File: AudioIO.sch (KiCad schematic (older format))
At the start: 39 parts, among them U4 TL074

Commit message: Chanced regulators and oscillator work.
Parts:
- C32: renamed from C17; footprint Capacitor_SMD:C_0603_1608Metric -> Capacitor_SMD:C_0402_1005Metric
- C33: renamed from C18; footprint Capacitor_SMD:C_0603_1608Metric -> Capacitor_SMD:C_0402_1005Metric
- C34: renamed from C19; footprint Capacitor_SMD:C_0603_1608Metric -> Capacitor_SMD:C_0402_1005Metric
- C35: renamed from C20; footprint Capacitor_SMD:C_0603_1608Metric -> Capacitor_SMD:C_0402_1005Metric
- renumbered C15 to C30, C16 to C31, C21 to C36, C22 to C37, C23 to C38, C24 to C39, C25 to C40, C26 to C41, C27 to C42, C28 to C43, R7 to R10, R8 to R11, R9 to R12, R10 to R13, R11 to R14, R12 to R15, R13 to R16, R14 to R17, R15 to R18, R16 to R19, R17 to R20, R18 to R21, R19 to R22, R20 to R23, R21 to R24, R22 to R25, R3 to R6, R4 to R7, R5 to R8, R6 to R9, U4 to U5

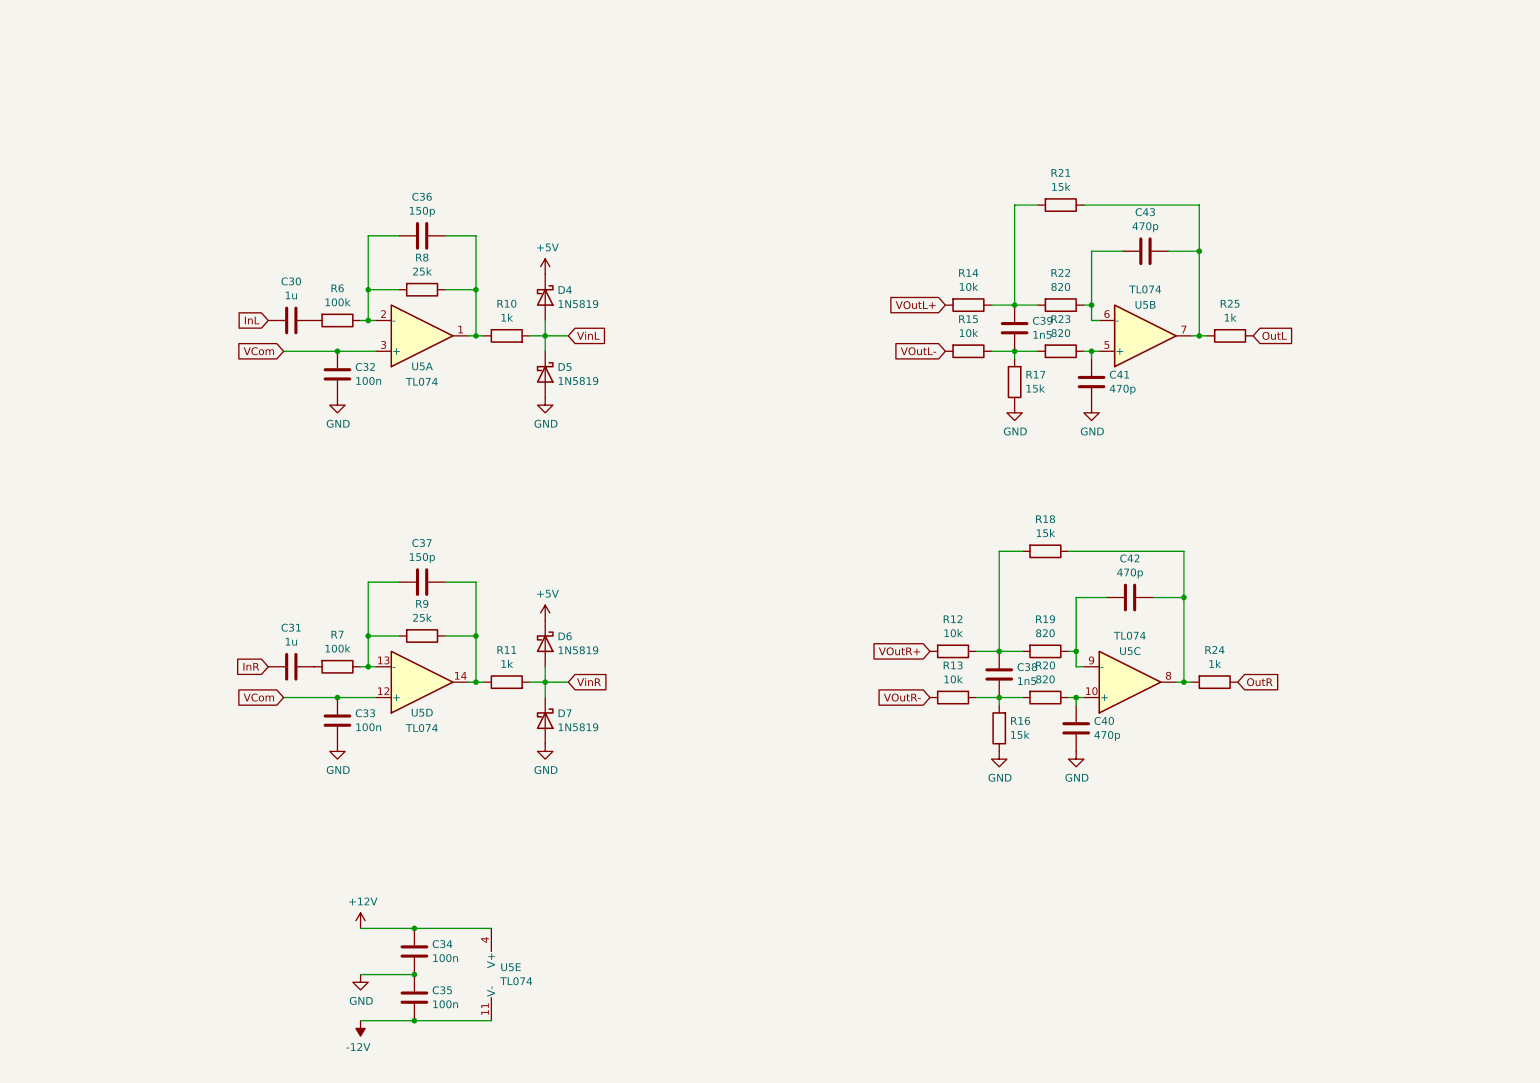
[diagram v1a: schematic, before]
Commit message: Added UI components.
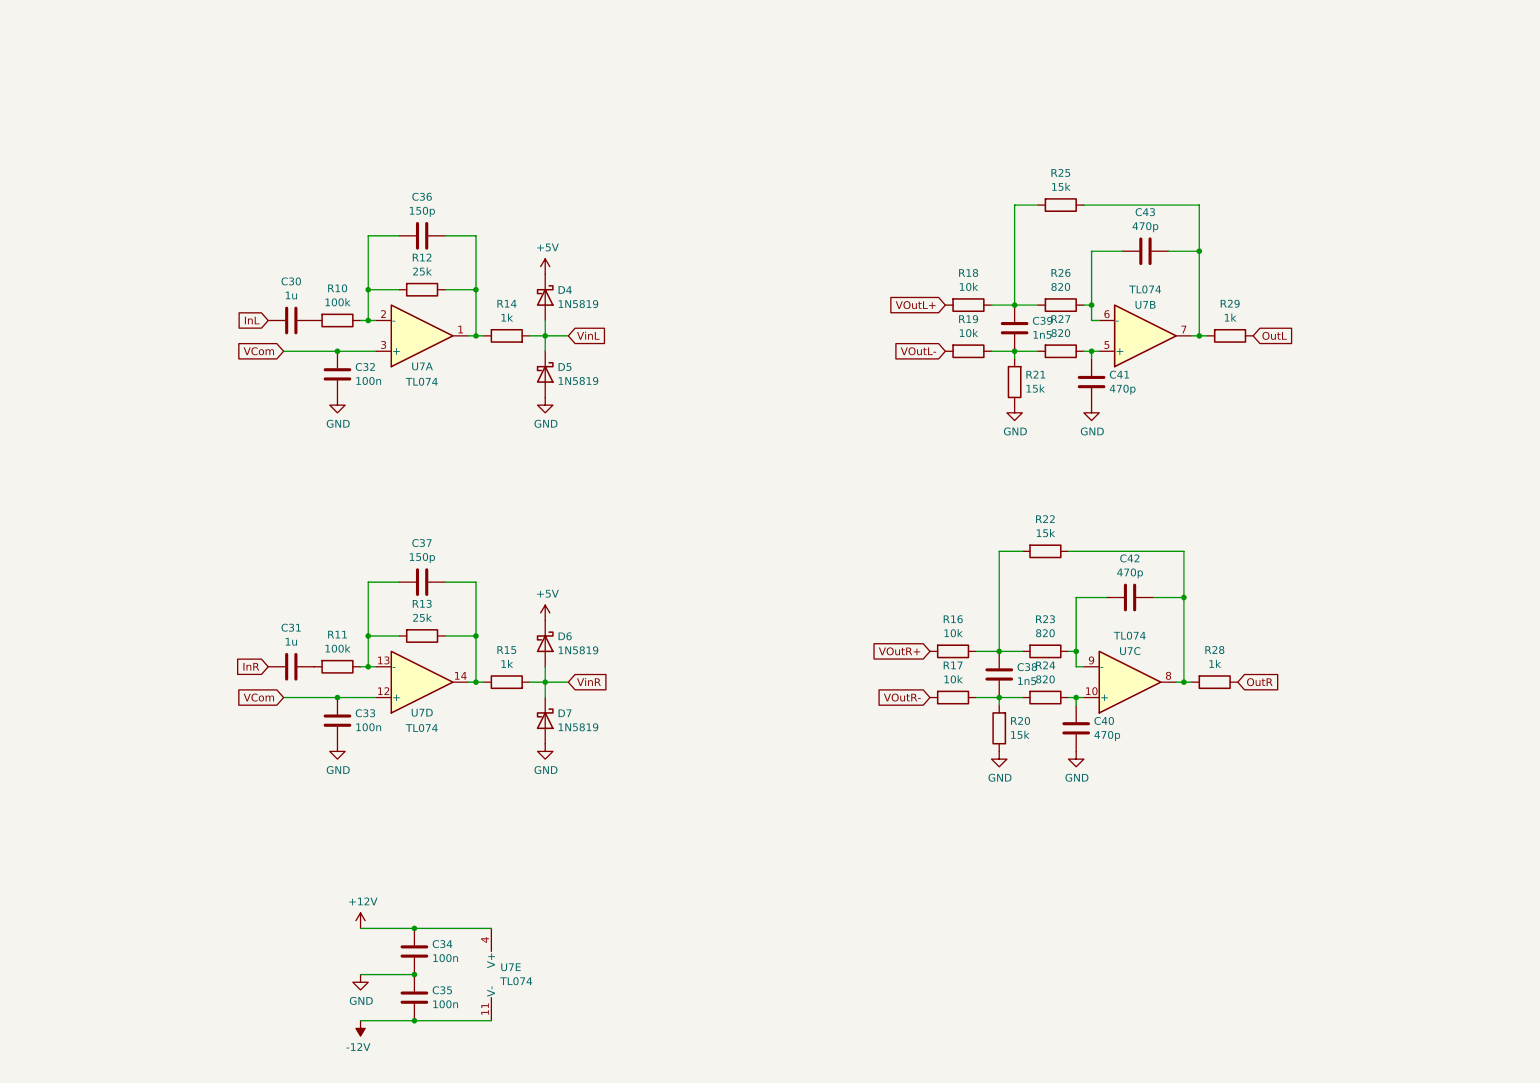
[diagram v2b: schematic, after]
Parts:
- renumbered R6 to R10, R7 to R11, R8 to R12, R9 to R13, R10 to R14, R11 to R15, R12 to R16, R13 to R17, R14 to R18, R15 to R19, R16 to R20, R17 to R21, R18 to R22, R19 to R23, R20 to R24, R21 to R25, R22 to R26, R23 to R27, R24 to R28, R25 to R29, U5 to U7

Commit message: Moved codec to audio module.
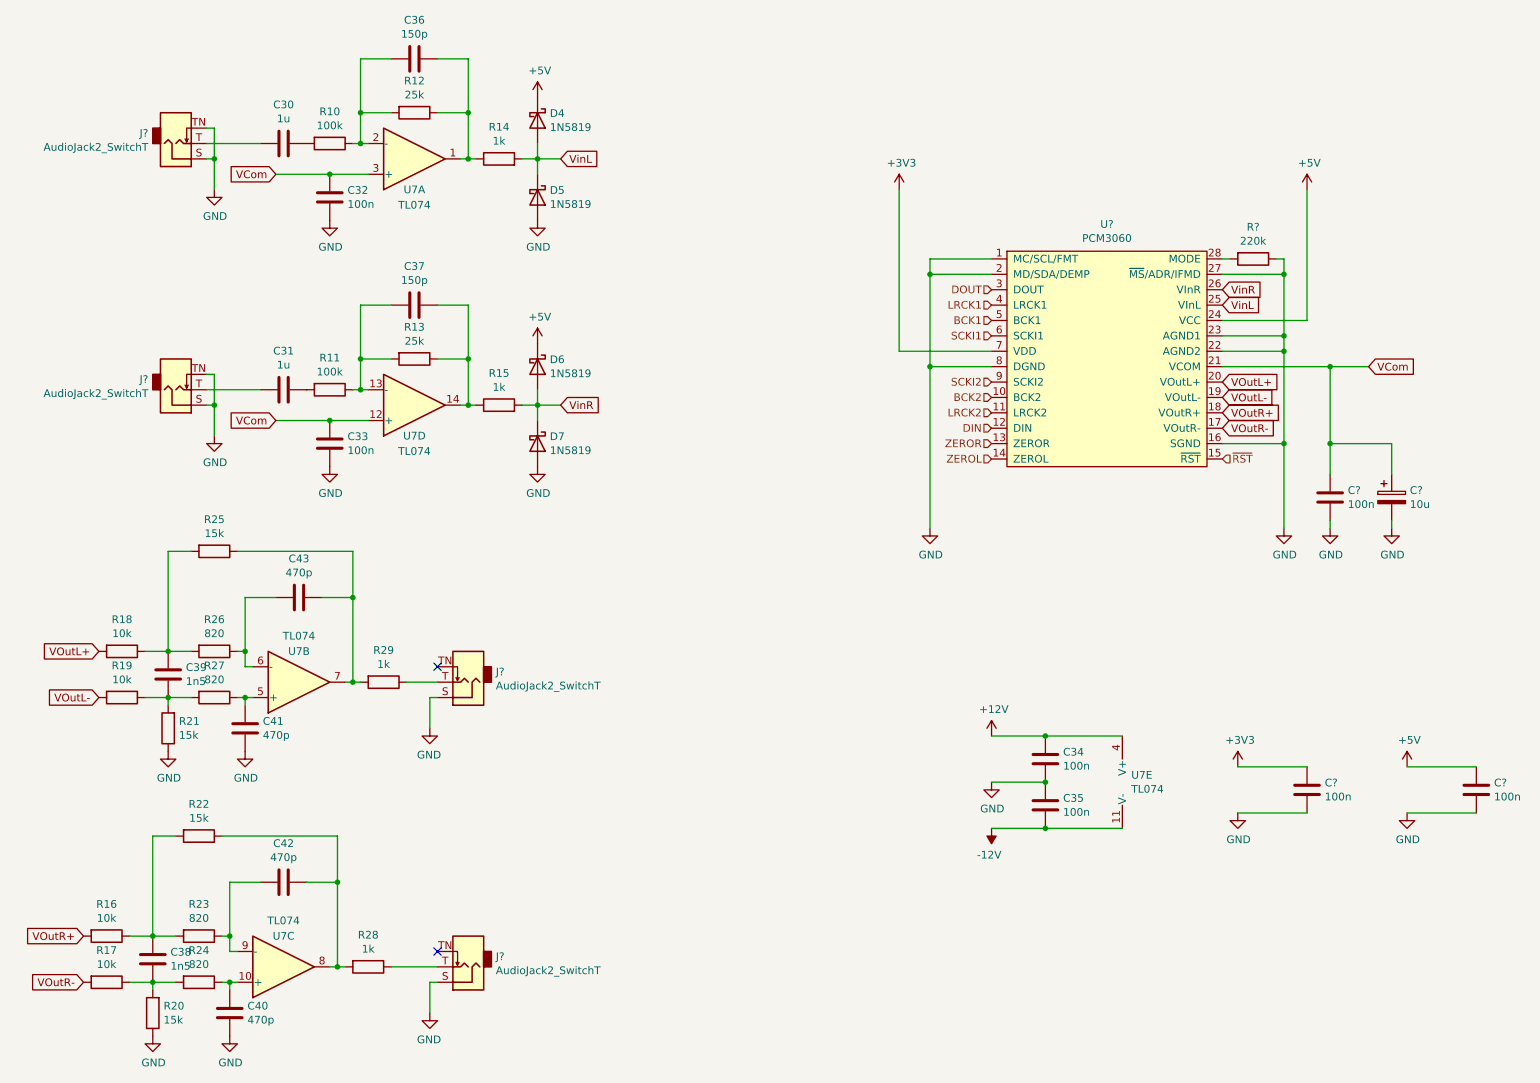
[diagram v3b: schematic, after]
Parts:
- added C? (x3): 100n, Capacitor_SMD:C_0402_1005Metric, symbol Device:C
- added C?: 10u, Capacitor_SMD:C_0603_1608Metric, symbol Device:CP
- added J? (x4): AudioJack2_SwitchT, Local:PJ398SM, symbol Connector:AudioJack2_SwitchT
- added R?: 220k, Resistor_SMD:R_0603_1608Metric, symbol Device:R
- added U?: PCM3060, Package_SO:TSSOP-28_4.4x9.7mm_P0.65mm, symbol PCM3060:PCM3060
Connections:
- net +5V: now also C?.1, U?.24 (VCC)
- net GND: now also C?.2, C?.2, C?.2, C?.2, J?.S, J?.S, J?.S, J?.S, J?.TN, J?.TN, R?.1, U?.1 (MC/SCL/FMT), U?.16 (SGND), U?.2 (MD/SDA/DEMP), U?.22 (AGND2), U?.23 (AGND1), U?.27 (~MS~/ADR/IFMD), U?.8 (DGND)
- net VCom: now also C?.1, C?.1, U?.21 (VCOM)
- net VOutL+: now also U?.20 (VOutL+)
- net VOutL-: now also U?.19 (VOutL-)
- net VOutR+: now also U?.18 (VOutR+)
- net VOutR-: now also U?.17 (VOutR-)
- net VinL: now also U?.25 (VInL)
- net VinR: now also U?.26 (VInR)
- net InL: no longer names the net of C30.2
- net InL: now also J?.T
- net InR: no longer names the net of C31.2
- net InR: now also J?.T
- net OutL: no longer names the net of R29.1
- net OutL: now also J?.T
- net OutR: no longer names the net of R28.1
- net OutR: now also J?.T
- new net: R?.2, U?.28 (MODE)
- new net +3V3: C?.1, U?.7 (VDD)
- new net BCK1: U?.5 (BCK1)
- new net BCK2: U?.10 (BCK2)
- new net DIN: U?.12 (DIN)
- new net DOUT: U?.3 (DOUT)
- new net LRCK1: U?.4 (LRCK1)
- new net LRCK2: U?.11 (LRCK2)
- new net SCKI1: U?.6 (SCKI1)
- new net SCKI2: U?.9 (SCKI2)
- new net ZEROL: U?.14 (ZEROL)
- new net ZEROR: U?.13 (ZEROR)
- new net ~RST: U?.15 (~RST)
- no-connect marks 0 -> 2
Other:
- moved on the sheet: C30, C31, C32, C33, C34, C35, C36, C37, C38, C39, C40, C41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

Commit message: Re-annotation.
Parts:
- gave numbers to parts that had none: 10
- renumbered C38 to C32, C39 to C33, C40 to C34, C41 to C35, C30 to C36, C31 to C37, C42 to C38, C43 to C39, C32 to C40, C33 to C41, C36 to C42, C37 to C43, C34 to C44, C35 to C45, R16 to R25, R17 to R26, R18 to R27, R19 to R28, R20 to R29, R21 to R30, R22 to R31, R23 to R32, R24 to R33, R25 to R34, R26 to R35, R27 to R36, R10 to R37, R11 to R38, R28 to R39, R29 to R40, R12 to R41, R13 to R42, R14 to R43, R15 to R44

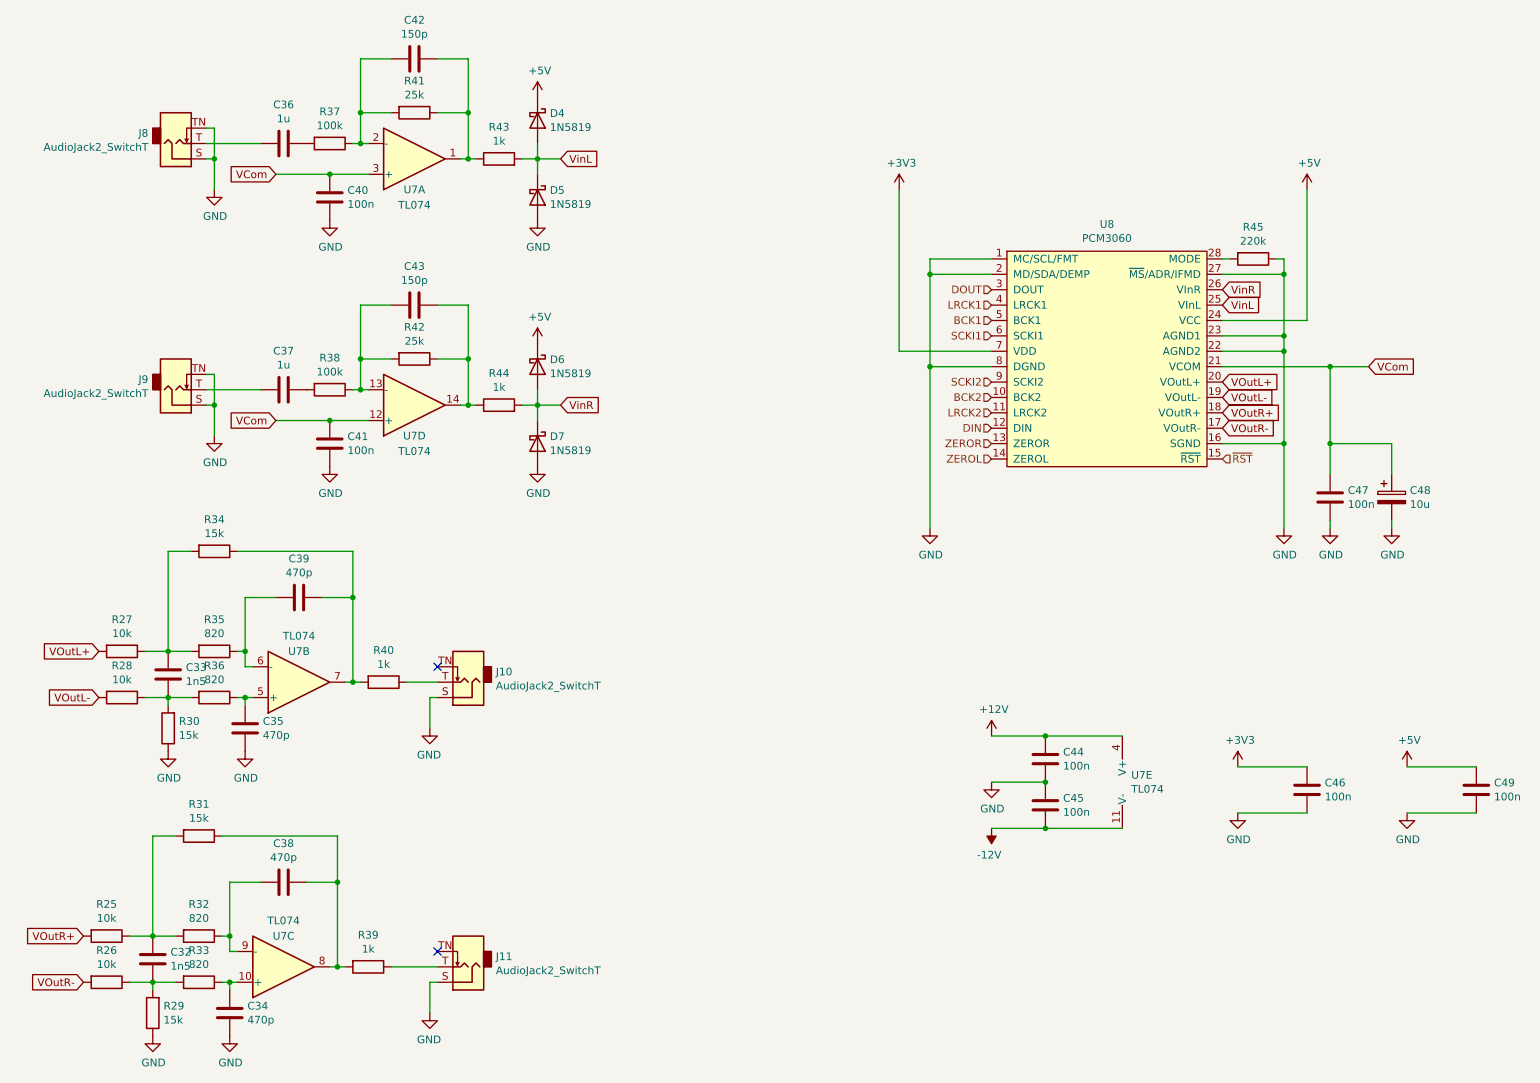
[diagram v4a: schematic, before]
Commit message: Assigned pins and cleared schema rules.
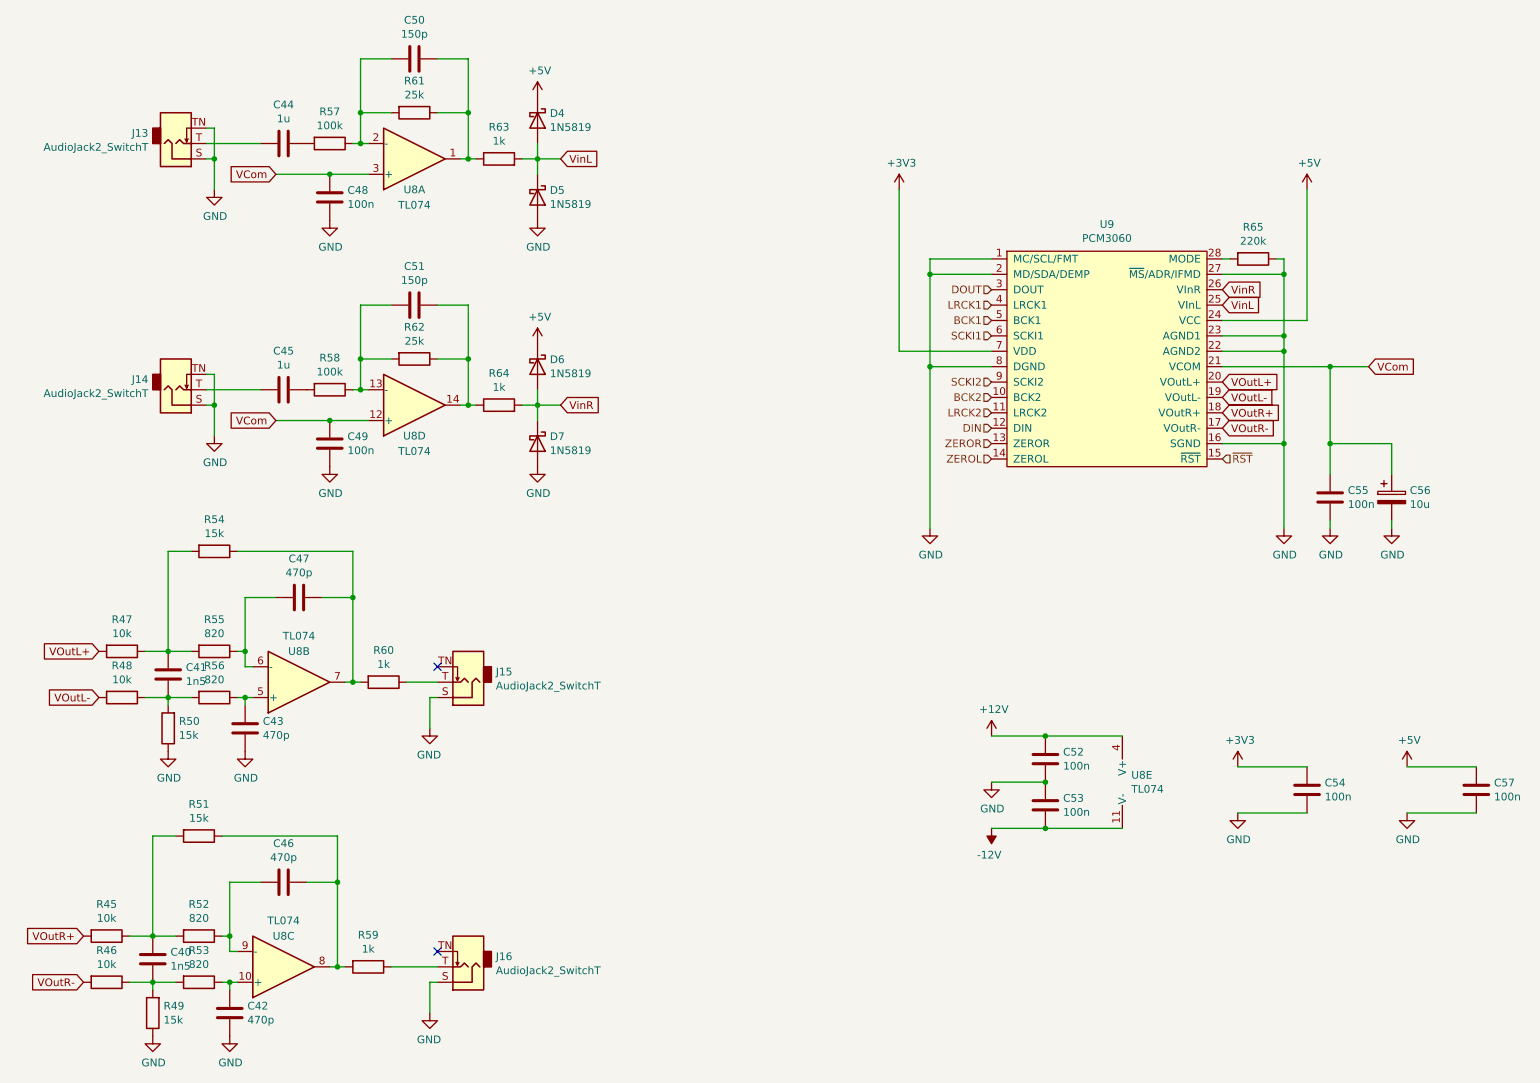
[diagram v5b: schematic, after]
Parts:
- renumbered C32 to C40, C33 to C41, C34 to C42, C35 to C43, C36 to C44, C37 to C45, C38 to C46, C39 to C47, C40 to C48, C41 to C49, C42 to C50, C43 to C51, C44 to C52, C45 to C53, C46 to C54, C47 to C55, C48 to C56, C49 to C57, J8 to J13, J9 to J14, J10 to J15, J11 to J16, R25 to R45, R26 to R46, R27 to R47, R28 to R48, R29 to R49, R30 to R50, R31 to R51, R32 to R52, R33 to R53, R34 to R54, R35 to R55, R36 to R56, R37 to R57, R38 to R58, R39 to R59, R40 to R60, R41 to R61, R42 to R62, R43 to R63, R44 to R64, R45 to R65, U7 to U8, U8 to U9
